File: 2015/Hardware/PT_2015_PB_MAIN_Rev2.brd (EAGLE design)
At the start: 139.7 x 170.8 mm, 135 parts, among them Q1 Q_ACS711LC, Q11 Q_IRFS7437PbF, Q12 2N7002, Q14 Q_IRFS7437PbF, Q16 Q_IRFS7437PbF, Q18 Q_FDT86102LZ, Q20 Q_IRFS7437PbF, Q4 Q_ACS711LC, Q5 Q_ACS711LC, Q6 Q_IRFS7437PbF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

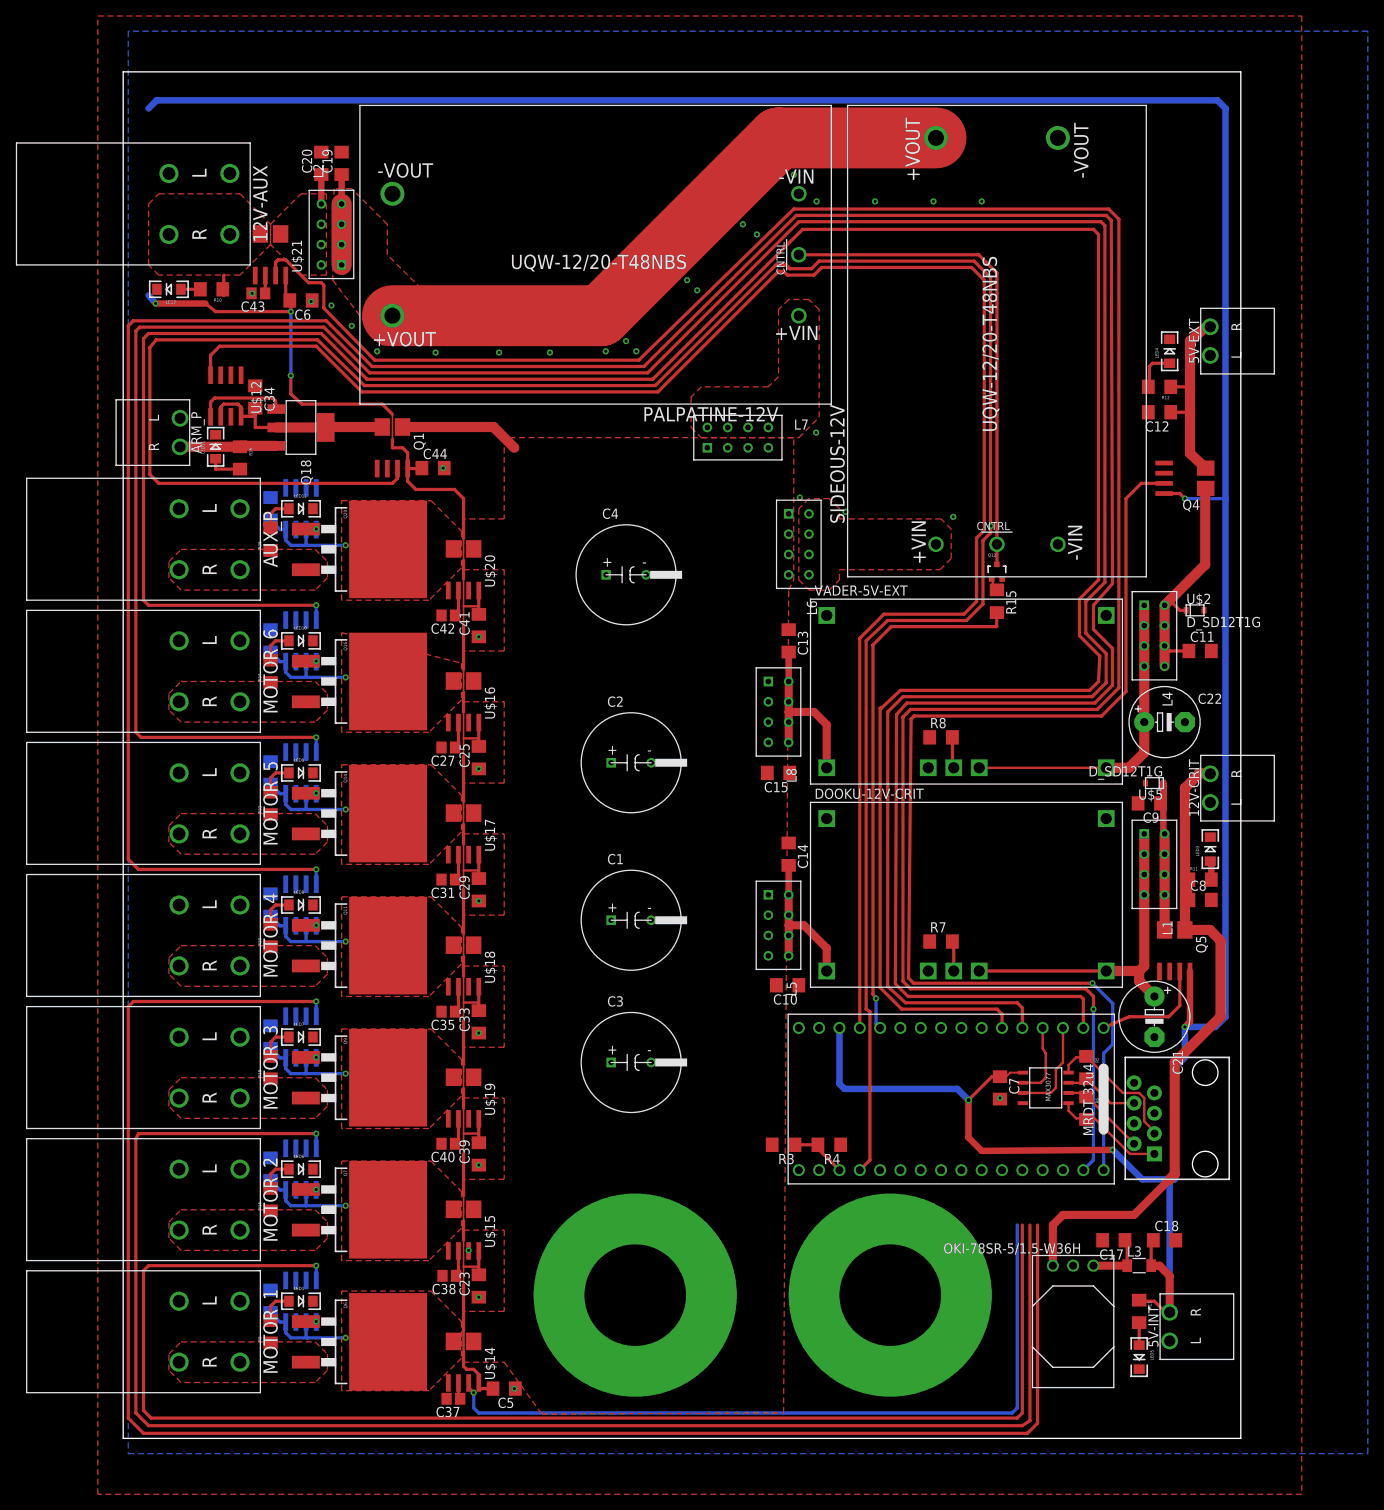
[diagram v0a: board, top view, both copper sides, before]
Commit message: Rerouted everything
Rerouted all analog signal and measurement lines for 3oz cu, unsure of
signal integrety being so close to MAJOR POWER ACTION MEGA TRACES. Also
remapped (correct word?) the 32u4 to be more easier to route.
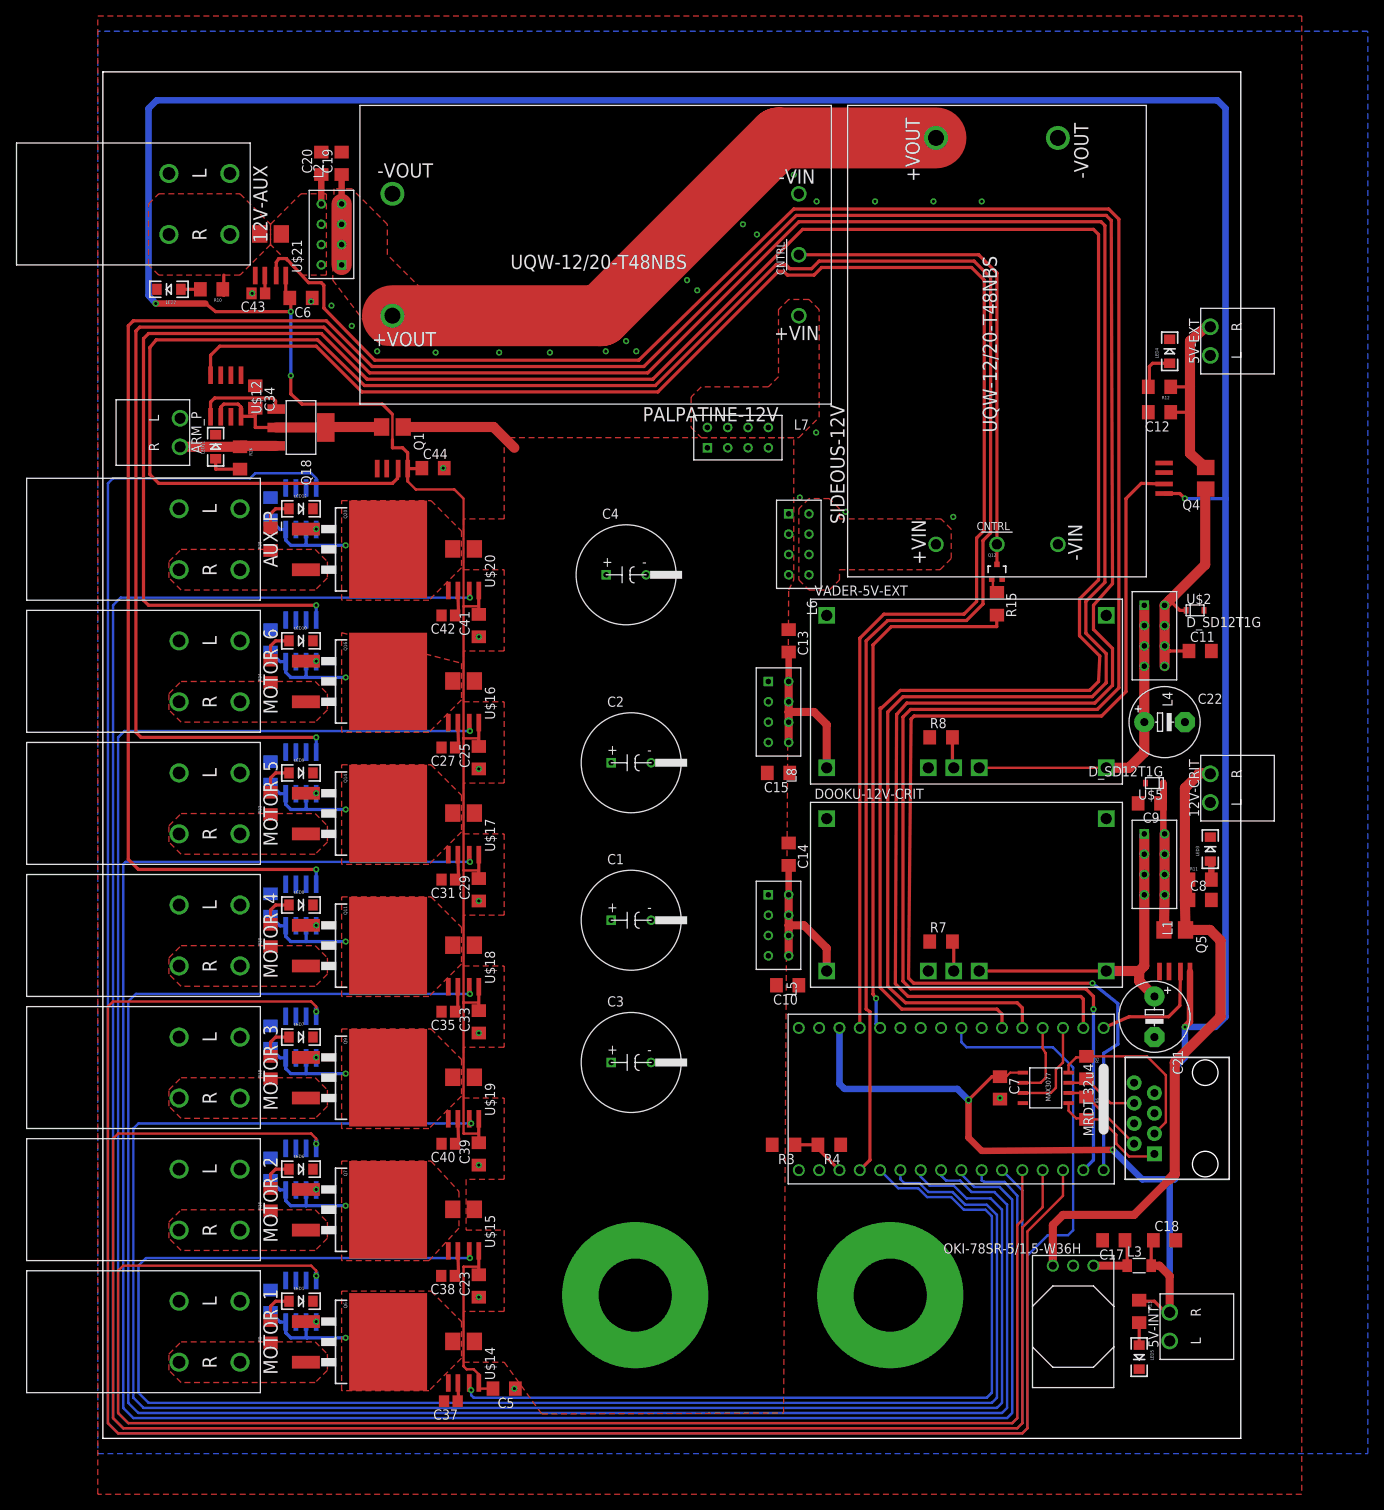
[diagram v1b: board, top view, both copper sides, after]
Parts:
- moved C37 0.45 mm to (39.1, 0.19)
- moved C6 0.32 mm to (20.3, 138.1)
- moved R15 0.32 mm to (107.3, 99.9)
- moved C38 0.16 mm to (38.7, 15.9)
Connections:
- net AUX_P-IMEAS: now also U$1.27; no longer U$1.21
- net M1-IMEAS: now also U$1.21; no longer U$1.28
- net M1-SIG: now also U$1.28; no longer U$1.25
- net M2-IMEAS: now also U$1.22; no longer U$1.29
- net M2-SIG: now also U$1.29; no longer U$1.26
- net M3-IMEAS: now also U$1.23; no longer U$1.30
- net M3-SIG: now also U$1.30; no longer U$1.27
- net M5-IMEAS: now also U$1.25; no longer U$1.23
- net M6-IMEAS: now also U$1.26; no longer U$1.22
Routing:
- net AUX_P-SIG: track 0.00 -> 327.2 mm
- net AUX_P-IMEAS: track 0.00 -> 294.6 mm, vias 0 -> 1
- net M6-IMEAS: track 0.00 -> 278.2 mm, vias 0 -> 1
- net M5-IMEAS: track 0.00 -> 259.1 mm, vias 0 -> 1
- net M4-IMEAS: track 0.00 -> 240.7 mm, vias 0 -> 1
- net M3-IMEAS: track 0.00 -> 223.0 mm, vias 0 -> 1
- net M2-IMEAS: track 0.00 -> 204.7 mm, vias 0 -> 1
- net M1-SIG: track 175.2 -> 188.7 mm
- net M2-SIG: track 196.1 -> 209.2 mm
- net M3-SIG: track 216.8 -> 229.7 mm
- net M1-IMEAS: track 94.7 -> 105.6 mm
- net +5V: track 606.3 -> 611.4 mm
- net N$20: track 18.0 -> 22.4 mm
- net 5V-IMEAS: track 138.5 -> 139.5 mm
- net N$14: track 14.0 -> 14.8 mm
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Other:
- board size 139.7 x 170.8 mm -> 142.2 x 170.8 mm

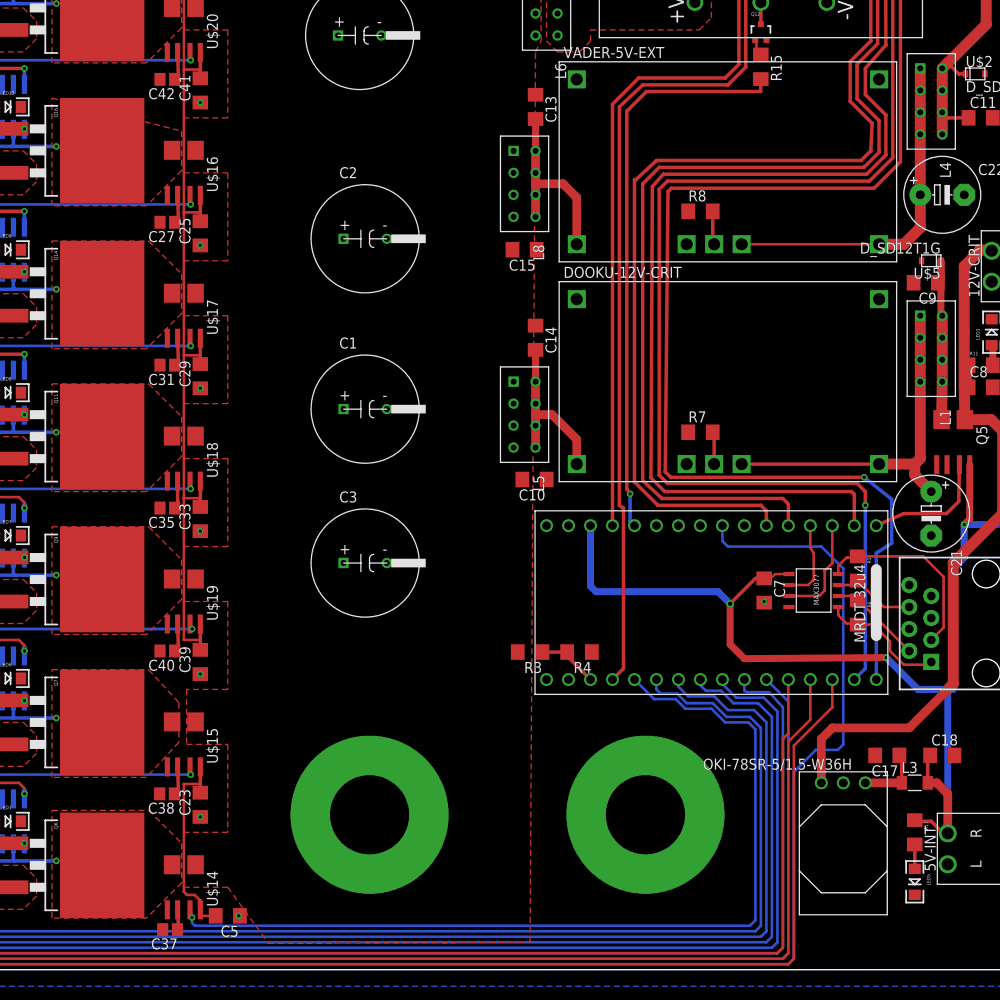
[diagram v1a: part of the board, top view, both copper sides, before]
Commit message: Fixed some minor polygon and trace errors
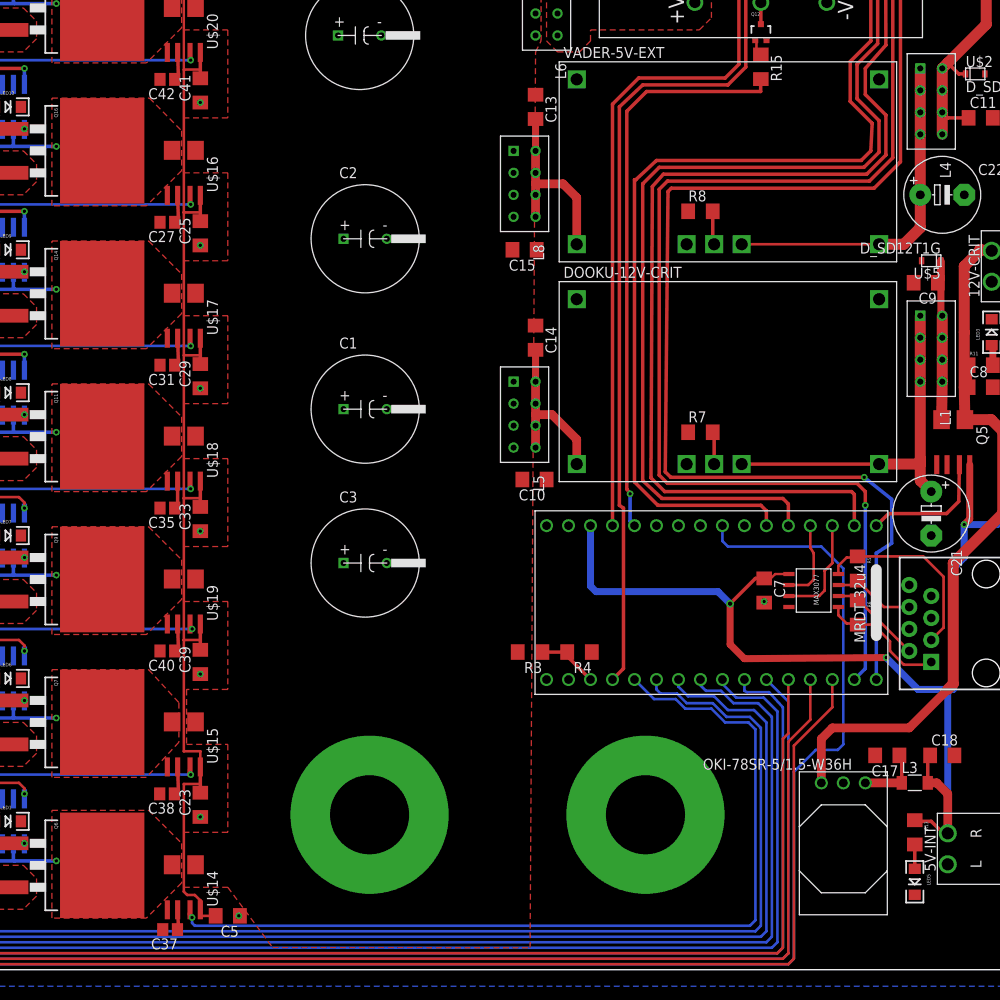
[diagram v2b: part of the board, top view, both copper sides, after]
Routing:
- net +5V: track 611.4 -> 628.0 mm
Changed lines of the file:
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@@
 <?xml version="1.0" encoding="utf-8"?>
 <!DOCTYPE eagle SYSTEM "eagle.dtd">
-<eagle version="6.5.0">
+<eagle version="7.0.0">
 <drawing>
 <settings>
@@
 <pass name="Default">
 <param name="RoutingGrid" value="50mil"/>
+<param name="AutoGrid" value="1"/>
+<param name="Efforts" value="0"/>
+<param name="TopRouterVariant" value="1"/>
 <param name="tpViaShape" value="round"/>
 <param name="PrefDir.1" value="|"/>
@@
 <vertex x="40.64" y="5.08"/>
 <vertex x="45.72" y="5.08"/>
-<vertex x="50.419" y="-1.397"/>
-<vertex x="80.645" y="-1.27"/>
+<vertex x="50.89525" y="-1.87325"/>
+<vertex x="80.645" y="-1.905"/>
 <vertex x="81.28" y="101.6"/>
 <vertex x="81.915" y="102.87"/>
@@
 <wire x1="1.27" y1="138.43" x2="1.27" y2="161.798" width="0.8128" layer="16"/>
 <wire x1="33.655" y1="116.78" x2="33.655" y2="117.602" width="0.3048" layer="1"/>
-<wire x1="42.545" y1="18.99" x2="42.545" y2="32.515" width="0" layer="19" extent="1-1"/>
+<wire x1="40.64" y1="33.655" x2="40.64" y2="20.79625" width="0.3048" layer="1"/>
+<wire x1="40.64" y1="20.79625" x2="42.545" y2="20.79625" width="0.3048" layer="1"/>
+<wire x1="42.545" y1="20.79625" x2="42.545" y2="18.99" width="0.3048" layer="1"/>
 </signal>
 <signal name="N$3">
@@
 <contactref element="C21" pad="+"/>
 <wire x1="105.095" y1="53.98" x2="120.975" y2="53.98" width="0.4064" layer="1"/>
-<wire x1="120.975" y1="53.98" x2="125.1" y2="53.98" width="1.27" layer="1"/>
-<wire x1="125.1" y1="53.98" x2="125.73" y2="54.61" width="1.27" layer="1"/>
+<wire x1="120.975" y1="53.98" x2="125.735" y2="53.98" width="1.27" layer="1"/>
+<wire x1="125.735" y1="53.98" x2="125.73" y2="54.61" width="1.27" layer="1"/>
 <wire x1="125.73" y1="54.61" x2="125.73" y2="63.5" width="1.27" layer="1"/>
 <wire x1="125.73" y1="63.5" x2="125.73" y2="66.04" width="1.27" layer="1"/>
 <wire x1="125.73" y1="66.04" x2="125.73" y2="68.58" width="1.27" layer="1"/>
 <wire x1="125.73" y1="68.58" x2="125.73" y2="71.12" width="1.27" layer="1"/>
-<wire x1="127" y1="50.8" x2="125.095" y2="52.715" width="1.27" layer="1"/>
-<wire x1="125.095" y1="52.715" x2="125.1" y2="53.98" width="1.27" layer="1"/>
+<wire x1="127" y1="50.8" x2="125.73" y2="52.08" width="1.27" layer="1"/>
+<wire x1="125.73" y1="52.08" x2="125.735" y2="53.98" width="1.27" layer="1"/>
 </signal>
 <signal name="N$9">
@@
 <contactref element="Q5" pad="7"/>
 <contactref element="U$1" pad="1"/>
-<wire x1="120.65" y1="46.863" x2="123.825" y2="48.26" width="0.4064" layer="1"/>
-<wire x1="123.825" y1="48.26" x2="128.778" y2="48.26" width="0.4064" layer="1"/>
+<wire x1="120.65" y1="46.863" x2="122.07875" y2="48.26" width="0.4064" layer="1"/>
+<wire x1="122.07875" y1="48.26" x2="128.778" y2="48.26" width="0.4064" layer="1"/>
 <wire x1="128.778" y1="48.26" x2="130.175" y2="49.657" width="0.4064" layer="1"/>
 <wire x1="130.175" y1="49.657" x2="130.254375" y2="53.915" width="0.4064" layer="1"/>
@@
 <polygon width="0.2794" layer="1" thermals="no" rank="3">
 <vertex x="25.4" y="96.266"/>
-<vertex x="40.386" y="92.456"/>
+<vertex x="36.67125" y="96.266"/>
+<vertex x="40.386" y="92.48775"/>
 <vertex x="40.386" y="87.884"/>
 <vertex x="36.322" y="83.82"/>
